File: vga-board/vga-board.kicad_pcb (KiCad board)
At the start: 2 copper layers, 19 parts, among them U1 74HC244, U10 74HC163, U11 74LS158, U12 74HC163, U13 74HC163, U14 74HC163, U15 74HC163, U16 74HC163, U17 GAL22V10, U18 GAL22V10, U2 74HC244, U3 74HC244, U4 74HC373, U5 74HC373, U6 74HC373, U7 74HC373, U8 71256SA12TPG, U9 74LS166, X1 40MHz

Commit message: More on VGA
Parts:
- added U19: 74HC163, Package_DIP:DIP-16_W7.62mm_Socket, F.Cu at (183.5, 126.6)
- added U20: 74HC163, Package_DIP:DIP-16_W7.62mm_Socket, F.Cu at (207.0, 99.5)
- added U21: 74HC163, Package_DIP:DIP-16_W7.62mm_Socket, F.Cu at (230.5, 72.4)
- added U22: 74HC163, Package_DIP:DIP-16_W7.62mm_Socket, F.Cu at (218.8, 99.5)
- added U23: 74HC163, Package_DIP:DIP-16_W7.62mm_Socket, F.Cu at (242.3, 72.4)
- U12: value 74HC163 -> 74LS251
- U13, U14, U15: value 74HC163 -> 74HC244; footprint Package_DIP:DIP-16_W7.62mm_Socket -> Package_DIP:DIP-20_W7.62mm_Socket
- U16: value 74HC163 -> GAL22V10; footprint Package_DIP:DIP-16_W7.62mm_Socket -> Package_DIP:DIP-24_W7.62mm_Socket
- U2: value 74HC244 -> 74HC373
- U9: value 74LS166 -> 74HC244; footprint Package_DIP:DIP-16_W7.62mm_Socket -> Package_DIP:DIP-20_W7.62mm_Socket
- moved U11 164.7 mm to (171.8, 126.6)
- moved U3 140.8 mm to (183.5, 72.4)
- moved U18 139.8 mm to (124.8, 109.7)
- moved U10 135.8 mm to (195.3, 99.5)
- moved U7 131.2 mm to (171.8, 99.5)
- moved U2 126.6 mm to (171.8, 72.4)
- moved U12 125.1 mm to (160.0, 126.6)
- moved U5 124.4 mm to (136.5, 104.6)
- moved U4 123.4 mm to (160.0, 99.5)
- moved U8 117.9 mm to (124.8, 72.4)
- moved U6 113.6 mm to (148.3, 104.6)
- moved U15 113.6 mm to (218.8, 72.4)
- moved U9 109.7 mm to (195.3, 72.4)
- moved U13 109.7 mm to (183.5, 99.5)
- moved U14 109.7 mm to (207.0, 72.4)
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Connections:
- net Net-(U18-Pad18) renamed VBLANK
- U1 pad 10: Net-(U1-Pad10) -> GND
- U1 pad 20: Net-(U1-Pad20) -> +5V
- U10 pad 12: X2 -> CLK
- U10 pad 16: Net-(U10-Pad16) -> +5V
- U10 pad 8: Net-(U10-Pad8) -> GND
- U11 pad 16: Net-(U11-Pad16) -> +5V
- U11 pad 8: Net-(U11-Pad8) -> GND
- U12 pad 1: !VRST -> Net-(U12-Pad1)
- U12 pad 10: LINE_INC -> X1
- U12 pad 11: Y3 -> X0
- U12 pad 12: Y2 -> Net-(U12-Pad12)
- U12 pad 13: Y1 -> Net-(U12-Pad13)
- U12 pad 14: Y0 -> Net-(U12-Pad14)
- U12 pad 16: Net-(U12-Pad16) -> +5V
- U12 pad 2: VCLK -> Net-(U12-Pad2)
- U12 pad 3: GND -> Net-(U12-Pad3)
- U12 pad 4: GND -> Net-(U12-Pad4)
- U12 pad 5: GND -> PIXEL
- U12 pad 6: GND -> Net-(U12-Pad6)
- U12 pad 7: +5V -> GND
- U12 pad 8: Net-(U12-Pad8) -> GND
- U12 pad 9: +5V -> CLK
- U13 pad 1: !HRST -> CHAR_LATCH
- U13 pad 10: Net-(U10-Pad15) -> GND
- U13 pad 11: X7 -> Net-(U13-Pad11)
- U13 pad 12: X6 -> VA3
- U13 pad 13: X5 -> +5V
- U13 pad 14: X4 -> VA2
- U13 pad 15: Net-(U13-Pad15) -> GND
- U13 pad 16: Net-(U13-Pad16) -> VA1
- U13 pad 2: VCLK -> Y0
- U13 pad 3: GND -> VA12
- U13 pad 4: GND -> Y1
- U13 pad 5: GND -> VA13
- U13 pad 6: GND -> Y2
- U13 pad 7: +5V -> VA14
- U13 pad 8: Net-(U13-Pad8) -> Y3
- U13 pad 9: +5V -> Net-(U13-Pad9)
- U14 pad 1: !VRST -> !CC_MASTER
- U14 pad 10: Net-(U12-Pad15) -> GND
- U14 pad 11: Y7 -> Net-(U14-Pad11)
- U14 pad 12: Y6 -> VA11
- U14 pad 13: Y5 -> GND
- U14 pad 14: Y4 -> VA10
- U14 pad 15: Net-(U14-Pad15) -> COLOR
- U14 pad 16: Net-(U14-Pad16) -> VA9
- U14 pad 2: VCLK -> Y5
- U14 pad 3: GND -> VA12
- U14 pad 4: GND -> Y6
- U14 pad 5: GND -> VA13
- U14 pad 6: GND -> Y7
- U14 pad 7: +5V -> VA14
- U14 pad 8: Net-(U14-Pad8) -> Y8
- U14 pad 9: +5V -> Net-(U14-Pad9)
- U15 pad 1: !HRST -> !CPU_MASTER
- U15 pad 10: Net-(U13-Pad15) -> GND
- U15 pad 12: X10 -> VD3
- U15 pad 13: X9 -> Net-(U15-Pad13)
- U15 pad 14: X8 -> VD2
- U15 pad 15: Net-(U15-Pad15) -> D5
- U15 pad 16: Net-(U15-Pad16) -> VD1
- U15 pad 2: VCLK -> D0
- U15 pad 3: GND -> VD4
- U15 pad 4: GND -> D1
- U15 pad 5: GND -> VD5
- U15 pad 6: GND -> D2
- U15 pad 7: +5V -> Net-(U15-Pad7)
- U15 pad 8: Net-(U15-Pad8) -> D3
- U15 pad 9: +5V -> Net-(U15-Pad9)
- U16 pad 1: !VRST -> VCLK
- U16 pad 10: Net-(U14-Pad15) -> Net-(U16-Pad10)
- U16 pad 12: Y10 -> GND
- U16 pad 13: Y9 -> Net-(U16-Pad13)
- U16 pad 14: Y8 -> RELATCH
- U16 pad 15: Net-(U16-Pad15) -> FONT_LATCH
- U16 pad 16: Net-(U16-Pad16) -> !FONT_MASTER
- U16 pad 2: VCLK -> X0
- U16 pad 3: GND -> X1
- U16 pad 4: GND -> CLK
- U16 pad 5: GND -> A15
- U16 pad 6: GND -> R!W
- U16 pad 7: +5V -> Net-(U16-Pad7)
- U16 pad 9: +5V -> Net-(U16-Pad9)
- U17 pad 1: VCLK -> X0
- U17 pad 10: X8 -> X9
- U17 pad 11: X9 -> X10
- U17 pad 12: Net-(U17-Pad12) -> GND
- U17 pad 13: X10 -> Net-(U17-Pad13)
- U17 pad 16: Net-(U17-Pad16) -> LINE_INC
- U17 pad 17: Net-(U17-Pad17) -> !HRST
- U17 pad 18: Net-(U17-Pad18) -> HBLANK
- U17 pad 19: Net-(U17-Pad19) -> HSYNC
- U17 pad 2: X0 -> X1
- U17 pad 20: LINE_INC -> HBLANK_END
- U17 pad 21: !HRST -> HBLANK_START
- U17 pad 22: HBLANK -> HSYNC_END
- U17 pad 23: HSYNC -> HSYNC_START
- U17 pad 24: Net-(U17-Pad24) -> +5V
- U17 pad 3: X1 -> CLK
- U17 pad 4: X2 -> X3
- U17 pad 5: X3 -> X4
- U17 pad 6: X4 -> X5
- U17 pad 7: X5 -> X6
- U17 pad 8: X6 -> X7
- U17 pad 9: X7 -> X8
- U18 pad 1: VCLK -> Y0
- U18 pad 10: Y8 -> Y9
- U18 pad 11: Y9 -> Y10
- U18 pad 12: Net-(U18-Pad12) -> GND
- U18 pad 13: Y10 -> HBLANK
- U18 pad 16: Net-(U18-Pad16) -> BLANK
- U18 pad 17: Net-(U18-Pad17) -> !VRST
- U18 pad 19: Net-(U18-Pad19) -> VSYNC
- U18 pad 2: Y0 -> Y1
- U18 pad 20: !VRST -> VBLANK_END
- U18 pad 21: BLANK -> VBLANK_START
- U18 pad 22: VSYNC -> VSYNC_END
- U18 pad 23: HBLANK -> VSYNC_START
- U18 pad 24: Net-(U18-Pad24) -> +5V
- U18 pad 3: Y1 -> Y2
- U18 pad 4: Y2 -> Y3
- U18 pad 5: Y3 -> Y4
- U18 pad 6: Y4 -> Y5
- U18 pad 7: Y5 -> Y6
- U18 pad 8: Y6 -> Y7
- U18 pad 9: Y7 -> Y8
- U2 pad 1: !CPU_MASTER -> VCLK
- U2 pad 10: Net-(U2-Pad10) -> GND
- U2 pad 11: Net-(U2-Pad11) -> RELATCH
- U2 pad 12: VA11 -> Net-(U12-Pad15)
- U2 pad 13: A14 -> Net-(U2-Pad13)
- U2 pad 14: VA10 -> Net-(U2-Pad14)
- U2 pad 15: A13 -> Net-(U12-Pad14)
- U2 pad 16: VA9 -> Net-(U12-Pad13)
- U2 pad 17: A12 -> Net-(U2-Pad17)
- U2 pad 18: VA8 -> Net-(U2-Pad18)
- U2 pad 19: !CPU_MASTER -> Net-(U12-Pad12)
- U2 pad 2: A8 -> Net-(U12-Pad4)
- U2 pad 20: Net-(U2-Pad20) -> +5V
- U2 pad 3: VA12 -> Net-(U2-Pad3)
- U2 pad 4: A9 -> Net-(U2-Pad4)
- U2 pad 5: VA13 -> Net-(U12-Pad3)
- U2 pad 6: A10 -> Net-(U12-Pad2)
- U2 pad 7: VA14 -> Net-(U2-Pad7)
- U2 pad 8: A11 -> Net-(U2-Pad8)
- U2 pad 9: Net-(U2-Pad9) -> Net-(U12-Pad1)
- U3 pad 1: !CPU_MASTER -> !CC_MASTER
- U3 pad 10: Net-(U3-Pad10) -> GND
- U3 pad 11: Net-(U3-Pad11) -> Y4
- U3 pad 12: VD3 -> VA3
- U3 pad 13: Net-(U3-Pad13) -> X9
- U3 pad 14: VD2 -> VA2
- U3 pad 15: D5 -> X8
- U3 pad 16: VD1 -> VA1
- U3 pad 17: D4 -> X7
- U3 pad 18: VD0 -> VA0
- U3 pad 19: !CPU_MASTER -> !CC_MASTER
- U3 pad 2: D0 -> X3
- U3 pad 20: Net-(U3-Pad20) -> +5V
- U3 pad 3: VD4 -> VA4
- U3 pad 4: D1 -> X4
- U3 pad 5: VD5 -> VA5
- U3 pad 6: D2 -> X5
- U3 pad 7: Net-(U3-Pad7) -> VA6
- U3 pad 8: D3 -> X6
- U3 pad 9: Net-(U3-Pad9) -> VA7
- U4 pad 1: Net-(U4-Pad1) -> !FONT_MASTER
- U4 pad 10: Net-(U4-Pad10) -> GND
- U4 pad 11: Net-(U4-Pad11) -> CHAR_LATCH
- U4 pad 20: Net-(U4-Pad20) -> +5V
- U5 pad 1: Net-(U5-Pad1) -> GND
- U5 pad 10: Net-(U5-Pad10) -> GND
- U5 pad 11: Net-(U5-Pad11) -> COLOR_LATCH
- U5 pad 20: Net-(U5-Pad20) -> +5V
- U6 pad 1: Net-(U6-Pad1) -> GND
- U6 pad 10: Net-(U6-Pad10) -> GND
- U6 pad 11: Net-(U6-Pad11) -> FONT_LATCH
- U6 pad 12: Net-(U6-Pad12) -> Net-(U2-Pad13)
- U6 pad 15: Net-(U6-Pad15) -> Net-(U2-Pad14)
- U6 pad 16: Net-(U6-Pad16) -> Net-(U2-Pad17)
- U6 pad 19: Net-(U6-Pad19) -> Net-(U2-Pad18)
- U6 pad 2: Net-(U6-Pad2) -> Net-(U2-Pad3)
- U6 pad 20: Net-(U6-Pad20) -> +5V
- U6 pad 5: Net-(U6-Pad5) -> Net-(U2-Pad4)
- U6 pad 6: Net-(U6-Pad6) -> Net-(U2-Pad7)
- U6 pad 9: Net-(U6-Pad9) -> Net-(U2-Pad8)
- U7 pad 1: Net-(U7-Pad1) -> GND
- U7 pad 10: Net-(U7-Pad10) -> GND
- U7 pad 11: Net-(U7-Pad11) -> RELATCH
- U7 pad 20: Net-(U7-Pad20) -> +5V
- U8 pad 14: Net-(U8-Pad14) -> GND
- U8 pad 22: !VID_MASTER -> CPU_MASTER
- U8 pad 27: !VRAM_WRITE_L -> !VRAM_WRITE
- U8 pad 28: Net-(U8-Pad28) -> +5V
- U9 pad 1: Net-(U9-Pad1) -> !CPU_MASTER
- U9 pad 10: Net-(U6-Pad12) -> GND
- U9 pad 11: Net-(U6-Pad15) -> Net-(U9-Pad11)
- U9 pad 12: Net-(U6-Pad16) -> VA11
- U9 pad 13: PIXEL -> A14
- U9 pad 14: Net-(U6-Pad19) -> VA10
- U9 pad 15: Net-(U9-Pad15) -> A13
- U9 pad 16: Net-(U9-Pad16) -> VA9
- U9 pad 2: Net-(U6-Pad2) -> A8
- U9 pad 3: Net-(U6-Pad5) -> VA12
- U9 pad 4: Net-(U6-Pad6) -> A9
- U9 pad 5: Net-(U6-Pad9) -> VA13
- U9 pad 6: Net-(U9-Pad6) -> A10
- U9 pad 7: Net-(U9-Pad7) -> VA14
- U9 pad 8: Net-(U9-Pad8) -> A11
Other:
- board text added: "SVGA - Work in progress"

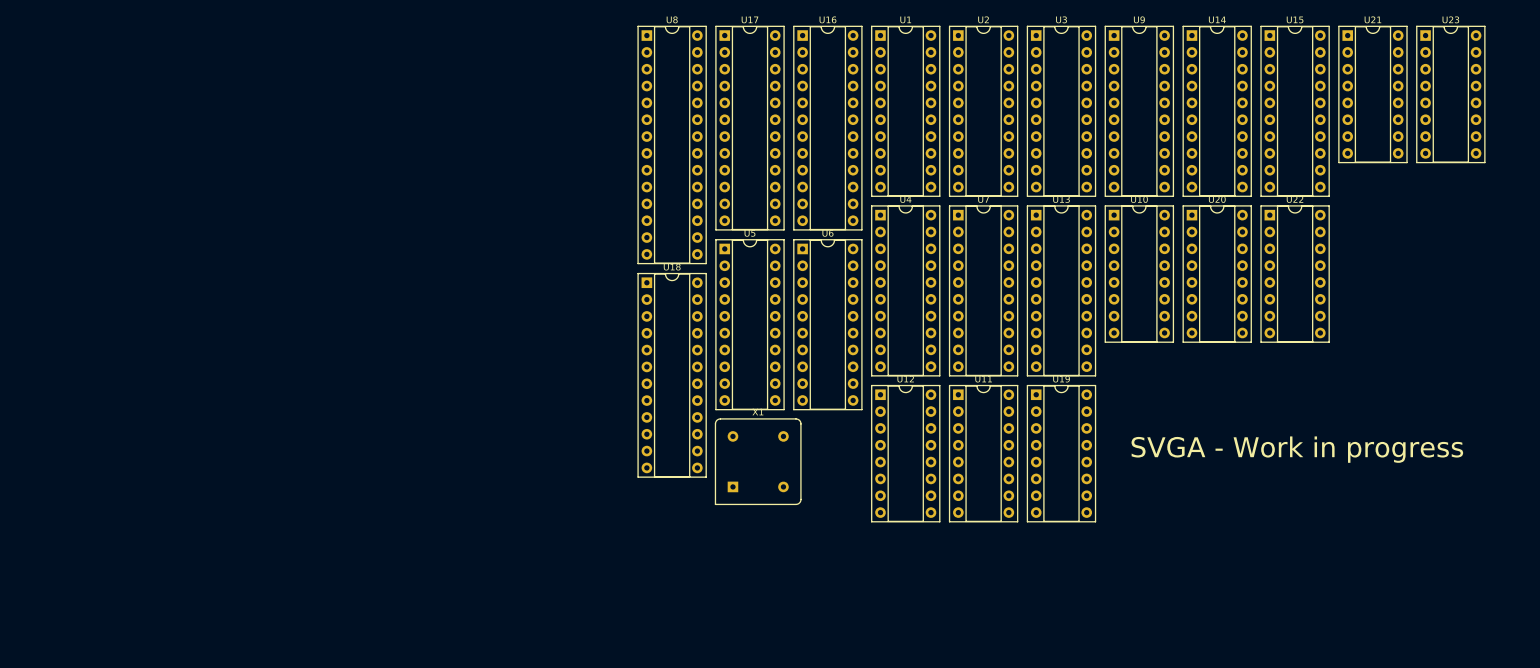
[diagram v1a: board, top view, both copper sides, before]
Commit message: Design new VGA board
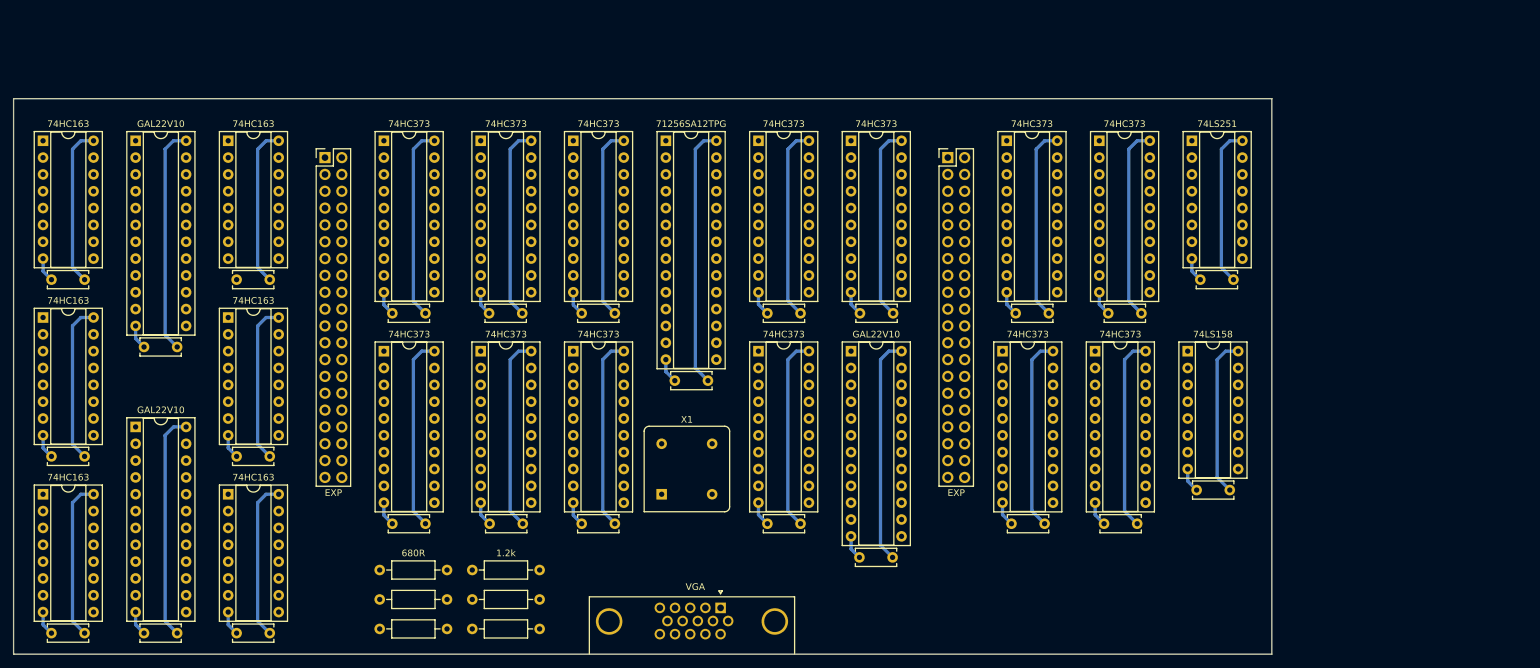
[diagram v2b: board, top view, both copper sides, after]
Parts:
- added C1: 0.1uF, Capacitor_THT:C_Disc_D6.0mm_W2.5mm_P5.00mm, F.Cu at (114.9, 114.3)
- added C10: 0.1uF, Capacitor_THT:C_Disc_D6.0mm_W2.5mm_P5.00mm, F.Cu at (86.4, 146.1)
- added C11: 0.1uF, Capacitor_THT:C_Disc_D6.0mm_W2.5mm_P5.00mm, F.Cu at (194.4, 114.3)
- added C12: 0.1uF, Capacitor_THT:C_Disc_D6.0mm_W2.5mm_P5.00mm, F.Cu at (62.9, 135.9)
- added C13: 0.1uF, Capacitor_THT:C_Disc_D6.0mm_W2.5mm_P5.00mm, F.Cu at (208.3, 109.2)
- added C14: 0.1uF, Capacitor_THT:C_Disc_D6.0mm_W2.5mm_P5.00mm, F.Cu at (34.9, 109.2)
- added C15: 0.1uF, Capacitor_THT:C_Disc_D6.0mm_W2.5mm_P5.00mm, F.Cu at (143.0, 114.3)
- added C16: 0.1uF, Capacitor_THT:C_Disc_D6.0mm_W2.5mm_P5.00mm, F.Cu at (180.4, 114.3)
- added C17: 0.1uF, Capacitor_THT:C_Disc_D6.0mm_W2.5mm_P5.00mm, F.Cu at (62.9, 109.2)
- added C18: 0.1uF, Capacitor_THT:C_Disc_D6.0mm_W2.5mm_P5.00mm, F.Cu at (129.0, 124.5)
- added C19: 0.1uF, Capacitor_THT:C_Disc_D6.0mm_W2.5mm_P5.00mm, F.Cu at (193.8, 146.1)
- added C2: 0.1uF, Capacitor_THT:C_Disc_D6.0mm_W2.5mm_P5.00mm, F.Cu at (34.9, 135.9)
- added C20: 0.1uF, Capacitor_THT:C_Disc_D6.0mm_W2.5mm_P5.00mm, F.Cu at (101.0, 146.1)
- added C21: 0.1uF, Capacitor_THT:C_Disc_D6.0mm_W2.5mm_P5.00mm, F.Cu at (156.8, 151.1)
- added C22: 0.1uF, Capacitor_THT:C_Disc_D6.0mm_W2.5mm_P5.00mm, F.Cu at (143.0, 146.1)
- added C23: 0.1uF, Capacitor_THT:C_Disc_D6.0mm_W2.5mm_P5.00mm, F.Cu at (114.9, 146.1)
- added C24: 0.1uF, Capacitor_THT:C_Disc_D6.0mm_W2.5mm_P5.00mm, F.Cu at (156.9, 114.3)
- added C25: 0.1uF, Capacitor_THT:C_Disc_D6.0mm_W2.5mm_P5.00mm, F.Cu at (179.8, 146.1)
- added C3: 0.1uF, Capacitor_THT:C_Disc_D6.0mm_W2.5mm_P5.00mm, F.Cu at (48.9, 162.6)
- added C4: 0.1uF, Capacitor_THT:C_Disc_D6.0mm_W2.5mm_P5.00mm, F.Cu at (34.9, 162.6)
- added C5: 0.1uF, Capacitor_THT:C_Disc_D6.0mm_W2.5mm_P5.00mm, F.Cu at (86.4, 114.3)
- added C6: 0.1uF, Capacitor_THT:C_Disc_D6.0mm_W2.5mm_P5.00mm, F.Cu at (48.9, 119.4)
- added C7: 0.1uF, Capacitor_THT:C_Disc_D6.0mm_W2.5mm_P5.00mm, F.Cu at (62.9, 162.6)
- added C8: 0.1uF, Capacitor_THT:C_Disc_D6.0mm_W2.5mm_P5.00mm, F.Cu at (101.0, 114.3)
- added C9: 0.1uF, Capacitor_THT:C_Disc_D6.0mm_W2.5mm_P5.00mm, F.Cu at (207.7, 141.0)
- added J1: EXP, Connector_PinHeader_2.54mm:PinHeader_2x20_P2.54mm_Vertical, F.Cu at (76.2, 90.8)
- added J2: EXP, Connector_PinHeader_2.54mm:PinHeader_2x20_P2.54mm_Vertical, F.Cu at (170.2, 90.8)
- added J3: VGA, Connector_Dsub:DSUB-15-HD_Female_Horizontal_P2.29x1.98mm_EdgePinOffset3.03mm_Housed_MountingHolesOffset4.94mm, F.Cu at (135.9, 158.8)
- added R1: 680R, Resistor_THT:R_Axial_DIN0207_L6.3mm_D2.5mm_P10.16mm_Horizontal, F.Cu at (84.5, 153.0)
- added R2: 1.2k, Resistor_THT:R_Axial_DIN0207_L6.3mm_D2.5mm_P10.16mm_Horizontal, F.Cu at (98.4, 153.0)
- added R3: 680R, Resistor_THT:R_Axial_DIN0207_L6.3mm_D2.5mm_P10.16mm_Horizontal, F.Cu at (84.5, 157.5)
- added R4: 1.2k, Resistor_THT:R_Axial_DIN0207_L6.3mm_D2.5mm_P10.16mm_Horizontal, F.Cu at (98.4, 157.5)
- added R5: 680R, Resistor_THT:R_Axial_DIN0207_L6.3mm_D2.5mm_P10.16mm_Horizontal, F.Cu at (84.5, 161.9)
- added R6: 1.2k, Resistor_THT:R_Axial_DIN0207_L6.3mm_D2.5mm_P10.16mm_Horizontal, F.Cu at (98.4, 161.9)
- added U24: 74HC373, Package_DIP:DIP-20_W7.62mm_Socket, F.Cu at (141.6, 88.3)
- added U25: 74HC373, Package_DIP:DIP-20_W7.62mm_Socket, F.Cu at (155.6, 88.3)
- U1: value 74HC244 -> GAL22V10; footprint Package_DIP:DIP-20_W7.62mm_Socket -> Package_DIP:DIP-24_W7.62mm_Socket
- U11: value 74LS158 -> 74HC373; footprint Package_DIP:DIP-16_W7.62mm_Socket -> Package_DIP:DIP-20_W7.62mm_Socket
- U12: value 74LS251 -> 74HC373; footprint Package_DIP:DIP-16_W7.62mm_Socket -> Package_DIP:DIP-20_W7.62mm_Socket
- U13, U14, U15: value 74HC244 -> 74HC373
- U16, U17, U18: value GAL22V10 -> 74HC373; footprint Package_DIP:DIP-24_W7.62mm_Socket -> Package_DIP:DIP-20_W7.62mm_Socket
- U19, U21, U22: value 74HC163 -> 74HC373; footprint Package_DIP:DIP-16_W7.62mm_Socket -> Package_DIP:DIP-20_W7.62mm_Socket
- U2, U4: value 74HC373 -> 74HC163; footprint Package_DIP:DIP-20_W7.62mm_Socket -> Package_DIP:DIP-16_W7.62mm_Socket
- U20: value 74HC163 -> 74LS251
- U23: value 74HC163 -> 74LS158
- U3, U9: value 74HC244 -> 74HC163; footprint Package_DIP:DIP-20_W7.62mm_Socket -> Package_DIP:DIP-16_W7.62mm_Socket
- U5: value 74HC373 -> 71256SA12TPG; footprint Package_DIP:DIP-20_W7.62mm_Socket -> Package_DIP:DIP-28_W7.62mm_Socket
- U6, U7: value 74HC373 -> GAL22V10; footprint Package_DIP:DIP-20_W7.62mm_Socket -> Package_DIP:DIP-24_W7.62mm_Socket
- U8: value 71256SA12TPG -> 74HC163; footprint Package_DIP:DIP-28_W7.62mm_Socket -> Package_DIP:DIP-16_W7.62mm_Socket
- moved U3 155.8 mm to (33.7, 114.9)
- moved U9 140.3 mm to (61.6, 114.9)
- moved U10 140.2 mm to (61.6, 141.6)
- moved U2 139.0 mm to (33.7, 88.3)
- moved U15 134.6 mm to (85.1, 88.3)
- moved U4 133.2 mm to (33.7, 141.6)
- moved U7 128.2 mm to (47.6, 131.4)
- moved U14 117.4 mm to (99.7, 120.0)
- moved U1 113.5 mm to (47.6, 88.3)
- moved U13 84.6 mm to (99.7, 88.3)
- moved U16 79.1 mm to (85.1, 120.0)
- moved U21 70.6 mm to (178.4, 120.0)
- moved U11 69.6 mm to (113.7, 88.3)
- moved U8 65.1 mm to (61.6, 88.3)
- moved U23 59.6 mm to (206.4, 120.0)
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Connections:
- U1 pad 1: !CPU_MASTER -> X0
- U1 pad 10: GND -> X9
- U1 pad 11: A7 -> X10
- U1 pad 12: VA3 -> GND
- U1 pad 13: A6 -> VBLANK
- U1 pad 14: VA2 -> Net-(U1-Pad14)
- U1 pad 15: A5 -> Net-(U1-Pad15)
- U1 pad 16: VA1 -> Net-(U1-Pad16)
- U1 pad 17: A4 -> Net-(U1-Pad17)
- U1 pad 18: VA0 -> Net-(U1-Pad18)
- U1 pad 19: !CPU_MASTER -> Net-(U1-Pad19)
- U1 pad 2: A0 -> X1
- U1 pad 20: +5V -> LINE_INC
- U1 pad 3: VA4 -> CLK
- U1 pad 4: A1 -> X3
- U1 pad 5: VA5 -> X4
- U1 pad 6: A2 -> X5
- U1 pad 7: VA6 -> X6
- U1 pad 8: A3 -> X7
- U1 pad 9: VA7 -> X8
- U10 pad 1: !HRST -> !VRST
- U10 pad 10: +5V -> Net-(U10-Pad10)
- U10 pad 11: X3 -> Net-(U10-Pad11)
- U10 pad 12: CLK -> Y10
- U10 pad 13: X1 -> Y9
- U10 pad 14: X0 -> Y8
- U11 pad 1: PIXEL -> !CC_MASTER
- U11 pad 10: BG_I -> GND
- U11 pad 11: FG_I -> +5V
- U11 pad 12: Net-(R3-Pad1) -> VA4
- U11 pad 13: BG_B -> X7
- U11 pad 14: FG_B -> X8
- U11 pad 15: BLANK -> VA5
- U11 pad 16: +5V -> VA6
- U11 pad 2: FG_R -> VA0
- U11 pad 3: BG_R -> X3
- U11 pad 4: Net-(R1-Pad1) -> X4
- U11 pad 5: FG_B -> VA1
- U11 pad 6: BG_G -> VA2
- U11 pad 7: Net-(R2-Pad1) -> X5
- U11 pad 8: GND -> X6
- U11 pad 9: Net-(R4-Pad2) -> VA3
- U12 pad 1: Net-(U12-Pad1) -> !CC_MASTER
- U12 pad 10: X1 -> GND
- U12 pad 11: X0 -> +5V
- U12 pad 12: Net-(U12-Pad12) -> VA12
- U12 pad 13: Net-(U12-Pad13) -> Y9
- U12 pad 14: Net-(U12-Pad14) -> COLOR
- U12 pad 15: Net-(U12-Pad15) -> VA13
- U12 pad 16: +5V -> VA14
- U12 pad 2: Net-(U12-Pad2) -> VA8
- U12 pad 3: Net-(U12-Pad3) -> Y5
- U12 pad 4: Net-(U12-Pad4) -> Y6
- U12 pad 5: PIXEL -> VA9
- U12 pad 6: Net-(U12-Pad6) -> VA10
- U12 pad 7: GND -> Y7
- U12 pad 8: GND -> Y8
- U12 pad 9: CLK -> VA11
- U13 pad 1: CHAR_LATCH -> !FONT_MASTER
- U13 pad 11: Net-(U13-Pad11) -> CHAR_LATCH
- U13 pad 12: VA3 -> VA4
- U13 pad 13: +5V -> VD0
- U13 pad 14: VA2 -> VD1
- U13 pad 15: GND -> VA5
- U13 pad 16: VA1 -> VA6
- U13 pad 17: GND -> VD2
- U13 pad 18: VA0 -> VD3
- U13 pad 19: !FONT_MASTER -> VA7
- U13 pad 2: Y0 -> VA0
- U13 pad 3: VA12 -> Y0
- U13 pad 5: VA13 -> VA1
- U13 pad 6: Y2 -> VA2
- U13 pad 7: VA14 -> Y2
- U13 pad 9: Net-(U13-Pad9) -> VA3
- U14 pad 1: !CC_MASTER -> !FONT_MASTER
- U14 pad 11: Net-(U14-Pad11) -> CHAR_LATCH
- U14 pad 12: VA11 -> VA12
- U14 pad 14: VA10 -> GND
- U14 pad 15: COLOR -> VA13
- U14 pad 16: VA9 -> VA14
- U14 pad 17: Y9 -> +5V
- U14 pad 18: VA8 -> Net-(U14-Pad18)
- U14 pad 19: !CC_MASTER -> Net-(U14-Pad19)
- U14 pad 2: Y5 -> VA8
- U14 pad 3: VA12 -> VD4
- U14 pad 4: Y6 -> VD5
- U14 pad 5: VA13 -> VA9
- U14 pad 6: Y7 -> VA10
- U14 pad 7: VA14 -> VD6
- U14 pad 8: Y8 -> VD7
- U14 pad 9: Net-(U14-Pad9) -> VA11
- U15 pad 11: Net-(U15-Pad11) -> +5V
- U15 pad 12: VD3 -> VA4
- U15 pad 13: Net-(U15-Pad13) -> A4
- U15 pad 14: VD2 -> A5
- U15 pad 15: D5 -> VA5
- U15 pad 16: VD1 -> VA6
- U15 pad 17: D4 -> A6
- U15 pad 18: VD0 -> A7
- U15 pad 19: !CPU_MASTER -> VA7
- U15 pad 2: D0 -> VA0
- U15 pad 3: VD4 -> A0
- U15 pad 4: D1 -> A1
- U15 pad 5: VD5 -> VA1
- U15 pad 6: D2 -> VA2
- U15 pad 7: Net-(U15-Pad7) -> A2
- U15 pad 8: D3 -> A3
- U15 pad 9: Net-(U15-Pad9) -> VA3
- U16 pad 1: VCLK -> !CPU_MASTER
- U16 pad 10: Net-(U16-Pad10) -> GND
- U16 pad 11: Net-(U16-Pad11) -> +5V
- U16 pad 12: GND -> VA12
- U16 pad 13: Net-(U16-Pad13) -> A12
- U16 pad 14: RELATCH -> A13
- U16 pad 15: FONT_LATCH -> VA13
- U16 pad 16: !FONT_MASTER -> VA14
- U16 pad 17: COLOR_LATCH -> A14
- U16 pad 18: CHAR_LATCH -> Net-(U16-Pad18)
- U16 pad 19: COLOR -> Net-(U16-Pad19)
- U16 pad 2: X0 -> VA8
- U16 pad 20: !CC_MASTER -> +5V
- U16 pad 3: X1 -> A8
- U16 pad 4: CLK -> A9
- U16 pad 5: A15 -> VA9
- U16 pad 6: R!W -> VA10
- U16 pad 7: Net-(U16-Pad7) -> A10
- U16 pad 8: Net-(U16-Pad8) -> A11
- U16 pad 9: Net-(U16-Pad9) -> VA11
- U17 pad 1: X0 -> !CPU_MASTER
- U17 pad 10: X9 -> GND
- U17 pad 11: X10 -> +5V
- U17 pad 12: GND -> VD4
- U17 pad 13: Net-(U17-Pad13) -> D4
- U17 pad 14: Net-(U17-Pad14) -> D5
- U17 pad 15: Net-(U17-Pad15) -> VD5
- U17 pad 16: LINE_INC -> Net-(U17-Pad16)
- U17 pad 17: !HRST -> Net-(U17-Pad17)
- U17 pad 18: HBLANK -> Net-(U17-Pad18)
- U17 pad 19: HSYNC -> Net-(U17-Pad19)
- U17 pad 2: X1 -> VD0
- U17 pad 20: HBLANK_END -> +5V
- U17 pad 3: CLK -> D0
- U17 pad 4: X3 -> D1
- U17 pad 5: X4 -> VD1
- U17 pad 6: X5 -> VD2
- U17 pad 7: X6 -> D2
- U17 pad 8: X7 -> D3
- U17 pad 9: X8 -> VD3
- U18 pad 1: Y0 -> GND
- U18 pad 10: Y9 -> GND
- U18 pad 11: Y10 -> FONT_LATCH
- U18 pad 12: GND -> Net-(U18-Pad12)
- U18 pad 13: HBLANK -> VD4
- U18 pad 14: Net-(U18-Pad14) -> VD5
- U18 pad 16: BLANK -> Net-(U18-Pad16)
- U18 pad 17: !VRST -> VD6
- U18 pad 18: VBLANK -> VD7
- U18 pad 19: VSYNC -> Net-(U18-Pad19)
- U18 pad 2: Y1 -> Net-(U18-Pad2)
- U18 pad 20: VBLANK_END -> +5V
- U18 pad 3: Y2 -> VD0
- U18 pad 4: Y3 -> VD1
- U18 pad 5: Y4 -> Net-(U18-Pad5)
- U18 pad 6: Y5 -> Net-(U18-Pad6)
- U18 pad 7: Y6 -> VD2
- U18 pad 8: Y7 -> VD3
- U18 pad 9: Y8 -> Net-(U18-Pad9)
- U19 pad 1: !VRST -> VCLK
- U19 pad 10: LINE_INC -> GND
- U19 pad 11: Y3 -> RELATCH
- U19 pad 12: Y2 -> Net-(U19-Pad12)
- U19 pad 13: Y1 -> Net-(U18-Pad12)
- U19 pad 14: Y0 -> Net-(U18-Pad15)
- U19 pad 16: +5V -> Net-(U19-Pad16)
- U19 pad 2: VCLK -> Net-(U19-Pad2)
- U19 pad 3: GND -> Net-(U18-Pad2)
- U19 pad 4: GND -> Net-(U18-Pad5)
- U19 pad 5: GND -> Net-(U19-Pad5)
- U19 pad 6: GND -> Net-(U19-Pad6)
- U19 pad 7: +5V -> Net-(U18-Pad6)
- U19 pad 8: GND -> Net-(U18-Pad9)
- U19 pad 9: +5V -> Net-(U19-Pad9)
- U2 pad 1: VCLK -> !HRST
- U2 pad 10: GND -> +5V
- U2 pad 11: RELATCH -> X3
- U2 pad 12: Net-(U12-Pad15) -> CLK
- U2 pad 13: Net-(U2-Pad13) -> X1
- U2 pad 14: Net-(U2-Pad14) -> X0
- U2 pad 15: Net-(U12-Pad14) -> Net-(U2-Pad15)
- U2 pad 16: Net-(U12-Pad13) -> +5V
- U2 pad 2: Net-(U12-Pad4) -> VCLK
- U2 pad 3: Net-(U2-Pad3) -> GND
- U2 pad 4: Net-(U2-Pad4) -> GND
- U2 pad 5: Net-(U12-Pad3) -> GND
- U2 pad 6: Net-(U12-Pad2) -> GND
- U2 pad 7: Net-(U2-Pad7) -> +5V
- U2 pad 8: Net-(U2-Pad8) -> GND
- U2 pad 9: Net-(U12-Pad1) -> +5V
- U20 pad 1: !HRST -> Net-(U19-Pad9)
- U20 pad 10: Net-(U10-Pad15) -> X1
- U20 pad 11: X7 -> X0
- U20 pad 12: X6 -> Net-(U19-Pad19)
- U20 pad 13: X5 -> Net-(U19-Pad16)
- U20 pad 14: X4 -> Net-(U19-Pad15)
- U20 pad 15: Net-(U20-Pad15) -> Net-(U19-Pad12)
- U20 pad 2: VCLK -> Net-(U19-Pad6)
- U20 pad 3: GND -> Net-(U19-Pad5)
- U20 pad 4: GND -> Net-(U19-Pad2)
- U20 pad 5: GND -> PIXEL
- U20 pad 6: GND -> Net-(U20-Pad6)
- U20 pad 7: +5V -> GND
- U20 pad 9: +5V -> CLK
- U21 pad 1: !VRST -> GND
- U21 pad 10: Net-(U19-Pad15) -> GND
- U21 pad 11: Y7 -> COLOR_LATCH
- U21 pad 12: Y6 -> Net-(U21-Pad12)
- U21 pad 13: Y5 -> VD4
- U21 pad 14: Y4 -> VD5
- U21 pad 16: +5V -> Net-(U21-Pad16)
- U21 pad 2: VCLK -> Net-(U21-Pad2)
- U21 pad 3: GND -> VD0
- U21 pad 4: GND -> VD1
- U21 pad 5: GND -> Net-(U21-Pad5)
- U21 pad 6: GND -> Net-(U21-Pad6)
- U21 pad 7: +5V -> VD2
- U21 pad 8: GND -> VD3
- U21 pad 9: +5V -> Net-(U21-Pad9)
- U22 pad 1: !HRST -> GND
- U22 pad 10: Net-(U20-Pad15) -> GND
- U22 pad 11: Net-(U22-Pad11) -> RELATCH
- U22 pad 12: X10 -> BG_R
- U22 pad 13: X9 -> Net-(U21-Pad12)
- U22 pad 14: X8 -> Net-(U21-Pad15)
- U22 pad 15: Net-(U22-Pad15) -> BG_G
- U22 pad 16: +5V -> BG_B
- U22 pad 2: VCLK -> FG_R
- U22 pad 3: GND -> Net-(U21-Pad2)
- U22 pad 4: GND -> Net-(U21-Pad5)
- U22 pad 5: GND -> FG_B
- U22 pad 6: GND -> FG_B
- U22 pad 7: +5V -> Net-(U21-Pad6)
- U22 pad 8: GND -> Net-(U21-Pad9)
- U22 pad 9: +5V -> FG_I
- U23 pad 1: !VRST -> PIXEL
- U23 pad 10: Net-(U21-Pad15) -> BG_I
- U23 pad 11: Net-(U23-Pad11) -> FG_I
- U23 pad 12: Y10 -> Net-(R5-Pad1)
- U23 pad 13: Y9 -> BG_B
- U23 pad 14: Y8 -> FG_B
- U23 pad 15: Net-(U23-Pad15) -> BLANK_OUT
- U23 pad 2: VCLK -> FG_R
- U23 pad 3: GND -> BG_R
- U23 pad 4: GND -> Net-(R1-Pad1)
- U23 pad 5: GND -> FG_B
- U23 pad 6: GND -> BG_G
- U23 pad 7: +5V -> Net-(R3-Pad1)
- U23 pad 9: +5V -> Net-(R2-Pad2)
- U3 pad 1: !CC_MASTER -> !HRST
- U3 pad 10: GND -> Net-(U2-Pad15)
- U3 pad 11: Y4 -> X7
- U3 pad 12: VA3 -> X6
- U3 pad 13: X9 -> X5
- U3 pad 14: VA2 -> X4
- U3 pad 15: X8 -> Net-(U3-Pad15)
- U3 pad 16: VA1 -> +5V
- U3 pad 2: X3 -> VCLK
- U3 pad 3: VA4 -> GND
- U3 pad 4: X4 -> GND
- U3 pad 5: VA5 -> GND
- U3 pad 6: X5 -> GND
- U3 pad 7: VA6 -> +5V
- U3 pad 8: X6 -> GND
- U3 pad 9: VA7 -> +5V
- U4 pad 1: !FONT_MASTER -> !HRST
- U4 pad 10: GND -> Net-(U3-Pad15)
- U4 pad 11: CHAR_LATCH -> Net-(U4-Pad11)
- U4 pad 12: VA8 -> X10
- U4 pad 13: VD4 -> X9
- U4 pad 14: VD5 -> X8
- U4 pad 15: VA9 -> Net-(U4-Pad15)
- U4 pad 16: VA10 -> +5V
- U4 pad 2: VA4 -> VCLK
- U4 pad 3: VD0 -> GND
- U4 pad 4: VD1 -> GND
- U4 pad 5: VA5 -> GND
- U4 pad 6: VA6 -> GND
- U4 pad 7: VD2 -> +5V
- U4 pad 8: VD3 -> GND
- U4 pad 9: VA7 -> +5V
- U5 pad 1: GND -> VA14
- U5 pad 10: GND -> VA0
- U5 pad 11: COLOR_LATCH -> VD0
- U5 pad 12: Net-(U5-Pad12) -> VD1
- U5 pad 13: VD4 -> VD2
- U5 pad 14: VD5 -> GND
- U5 pad 15: Net-(U5-Pad15) -> VD3
- U5 pad 16: Net-(U5-Pad16) -> VD4
- U5 pad 17: VD6 -> VD5
- U5 pad 18: VD7 -> VD6
- U5 pad 19: Net-(U5-Pad19) -> VD7
- U5 pad 2: Net-(U5-Pad2) -> VA12
- U5 pad 20: +5V -> GND
- U5 pad 3: VD0 -> VA7
- U5 pad 4: VD1 -> VA6
- U5 pad 5: Net-(U5-Pad5) -> VA5
- U5 pad 6: Net-(U5-Pad6) -> VA4
- U5 pad 7: VD2 -> VA3
- U5 pad 8: VD3 -> VA2
- U5 pad 9: Net-(U5-Pad9) -> VA1
- U6 pad 1: GND -> VCLK
- U6 pad 10: GND -> Net-(U6-Pad10)
- U6 pad 11: FONT_LATCH -> Net-(U6-Pad11)
- U6 pad 12: Net-(U2-Pad13) -> GND
- U6 pad 13: VD4 -> Net-(U6-Pad13)
- U6 pad 14: VD5 -> RELATCH
- U6 pad 15: Net-(U2-Pad14) -> FONT_LATCH
- U6 pad 16: Net-(U2-Pad17) -> !FONT_MASTER
- U6 pad 17: VD6 -> COLOR_LATCH
- U6 pad 18: VD7 -> CHAR_LATCH
- U6 pad 19: Net-(U2-Pad18) -> COLOR
- U6 pad 2: Net-(U2-Pad3) -> X0
- U6 pad 20: +5V -> !CC_MASTER
- U6 pad 3: VD0 -> X1
- U6 pad 4: VD1 -> CLK
- U6 pad 5: Net-(U2-Pad4) -> A15
- U6 pad 6: Net-(U2-Pad7) -> R!W
- U6 pad 7: VD2 -> Net-(U6-Pad7)
- U6 pad 8: VD3 -> Net-(U6-Pad8)
- U6 pad 9: Net-(U2-Pad8) -> Net-(U6-Pad9)
- U7 pad 1: GND -> Y0
- U7 pad 10: GND -> Y9
- U7 pad 11: RELATCH -> Y10
- U7 pad 12: BG_R -> GND
- U7 pad 13: Net-(U5-Pad12) -> Net-(U7-Pad13)
- U7 pad 14: Net-(U5-Pad15) -> Net-(U7-Pad14)
- U7 pad 15: BG_G -> Net-(U7-Pad15)
- U7 pad 16: BG_B -> Net-(U7-Pad16)
- U7 pad 17: Net-(U5-Pad16) -> Net-(U7-Pad17)
- U7 pad 18: Net-(U5-Pad19) -> Net-(U7-Pad18)
- U7 pad 19: BG_I -> Net-(U7-Pad19)
- U7 pad 2: FG_R -> Y1
- U7 pad 20: +5V -> Net-(U7-Pad20)
- U7 pad 3: Net-(U5-Pad2) -> Y2
- U7 pad 4: Net-(U5-Pad5) -> Y3
- U7 pad 5: FG_B -> Y4
- U7 pad 6: FG_B -> Y5
- U7 pad 7: Net-(U5-Pad6) -> Y6
- U7 pad 8: Net-(U5-Pad9) -> Y7
- U7 pad 9: FG_I -> Y8
- U8 pad 1: VA14 -> !VRST
- U8 pad 10: VA0 -> LINE_INC
- U8 pad 11: VD0 -> Y3
- U8 pad 12: VD1 -> Y2
- U8 pad 13: VD2 -> Y1
- U8 pad 14: GND -> Y0
- U8 pad 15: VD3 -> Net-(U8-Pad15)
- U8 pad 16: VD4 -> +5V
- U8 pad 2: VA12 -> VCLK
- U8 pad 3: VA7 -> GND
- U8 pad 4: VA6 -> GND
- U8 pad 5: VA5 -> GND
- U8 pad 6: VA4 -> GND
- U8 pad 7: VA3 -> +5V
- U8 pad 8: VA2 -> GND
- U8 pad 9: VA1 -> +5V
- U9 pad 1: !CPU_MASTER -> !VRST
- U9 pad 10: GND -> Net-(U8-Pad15)
- U9 pad 11: Net-(U9-Pad11) -> Y7
- U9 pad 12: VA11 -> Y6
- U9 pad 13: A14 -> Y5
- U9 pad 14: VA10 -> Y4
- U9 pad 15: A13 -> Net-(U10-Pad10)
- U9 pad 16: VA9 -> +5V
- U9 pad 2: A8 -> VCLK
- U9 pad 3: VA12 -> GND
- U9 pad 4: A9 -> GND
- U9 pad 5: VA13 -> GND
- U9 pad 6: A10 -> GND
- U9 pad 7: VA14 -> +5V
- U9 pad 8: A11 -> GND
- U9 pad 9: Net-(U9-Pad9) -> +5V
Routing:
- net +5V: track 0.00 -> 715.7 mm
- net GND: track 0.00 -> 89.2 mm
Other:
- board outline added: 189.9 x 83.8 mm
- net class Wide added: clearance 0.2, trace_width 0.5, via_dia 0.8, via_drill 0.4
- board text removed: "SVGA - Work in progress"

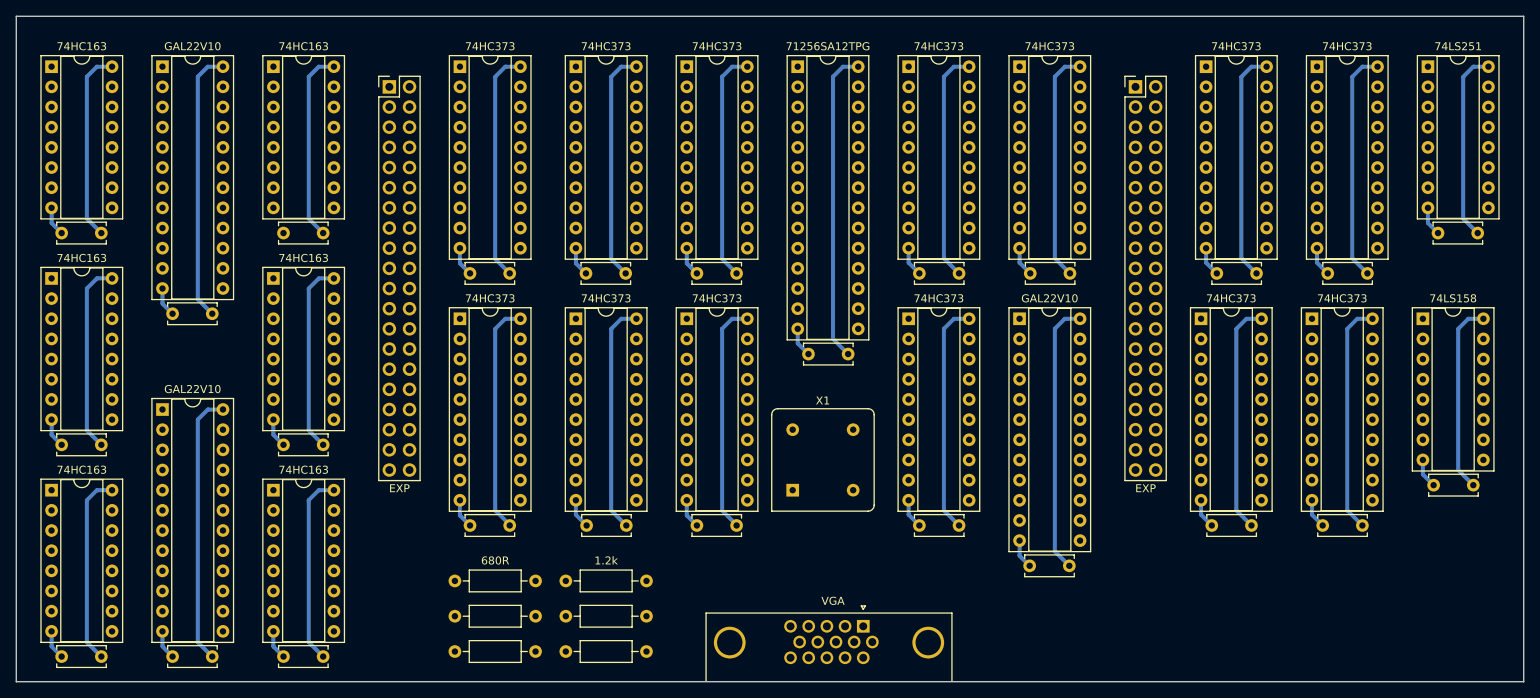
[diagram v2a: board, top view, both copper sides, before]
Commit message: Finish and route VGA board
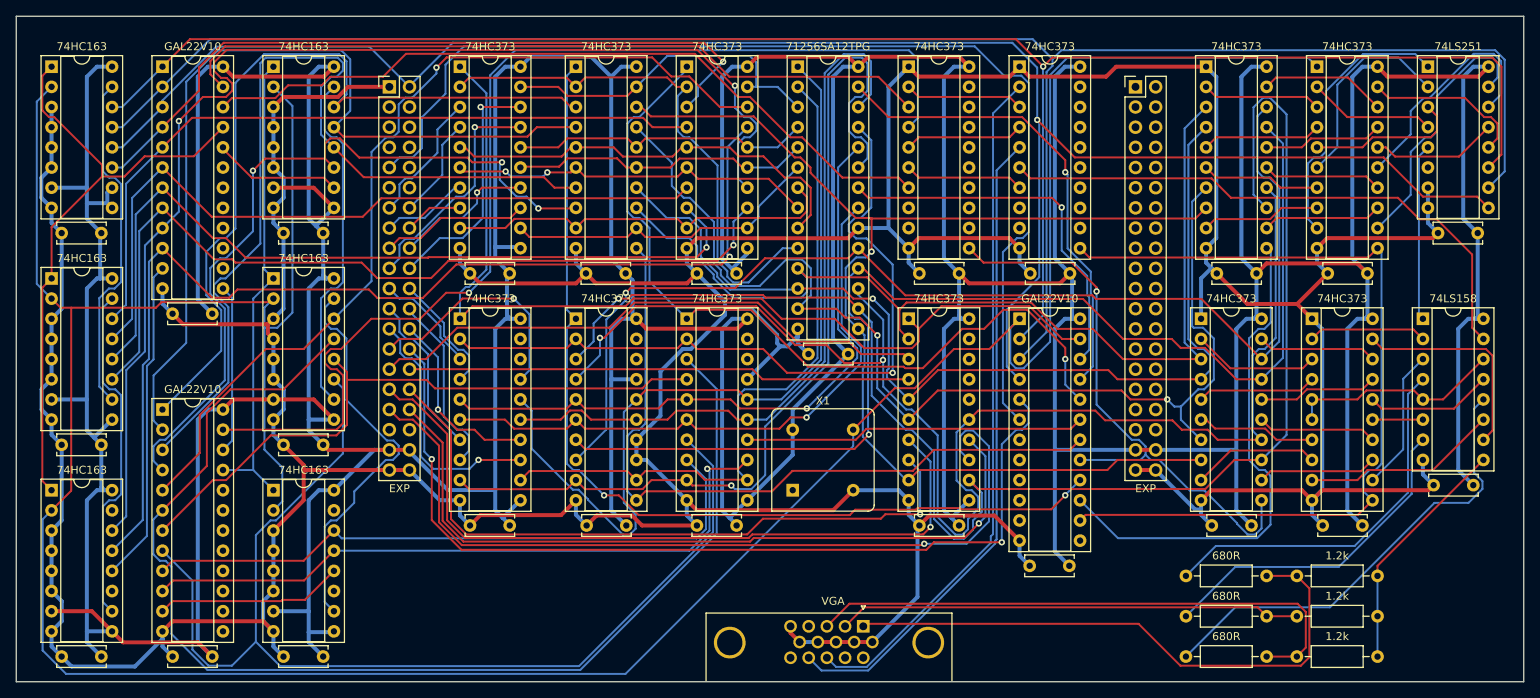
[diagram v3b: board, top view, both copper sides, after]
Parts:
- moved R1 92.1 mm to (176.5, 152.4)
- moved R2 92.1 mm to (190.5, 152.4)
- moved R5 92.1 mm to (176.5, 162.6)
- moved R6 92.1 mm to (190.5, 162.6)
- moved R3 92.1 mm to (176.5, 157.5)
- moved R4 92.1 mm to (190.5, 157.5)
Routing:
- net GND: track 89.2 -> 733.4 mm
- net VCLK: track 0.00 -> 389.4 mm
- net +5V: track 715.7 -> 1078.6 mm
- net X1: track 0.00 -> 238.5 mm
- net CLK: track 0.00 -> 231.1 mm, vias 0 -> 1
- net X0: track 0.00 -> 229.8 mm, vias 0 -> 1
- net VD4: track 0.00 -> 188.1 mm, vias 0 -> 1
- net VD5: track 0.00 -> 175.0 mm, vias 0 -> 2
- net VD3: track 0.00 -> 155.0 mm, vias 0 -> 1
- net Y5: track 0.00 -> 153.1 mm
- net X8: track 0.00 -> 152.7 mm, vias 0 -> 2
- net VD6: track 0.00 -> 151.3 mm, vias 0 -> 1
- net VD7: track 0.00 -> 146.6 mm, vias 0 -> 1
- net Y7: track 0.00 -> 141.4 mm
- net VD2: track 0.00 -> 140.9 mm, vias 0 -> 2
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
